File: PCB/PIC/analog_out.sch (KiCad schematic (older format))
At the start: 29 parts, among them J19 TB_1X2, Q1 PBSS5240XF, Q14 BC817-40, U18 LM358, U21 MCP6022

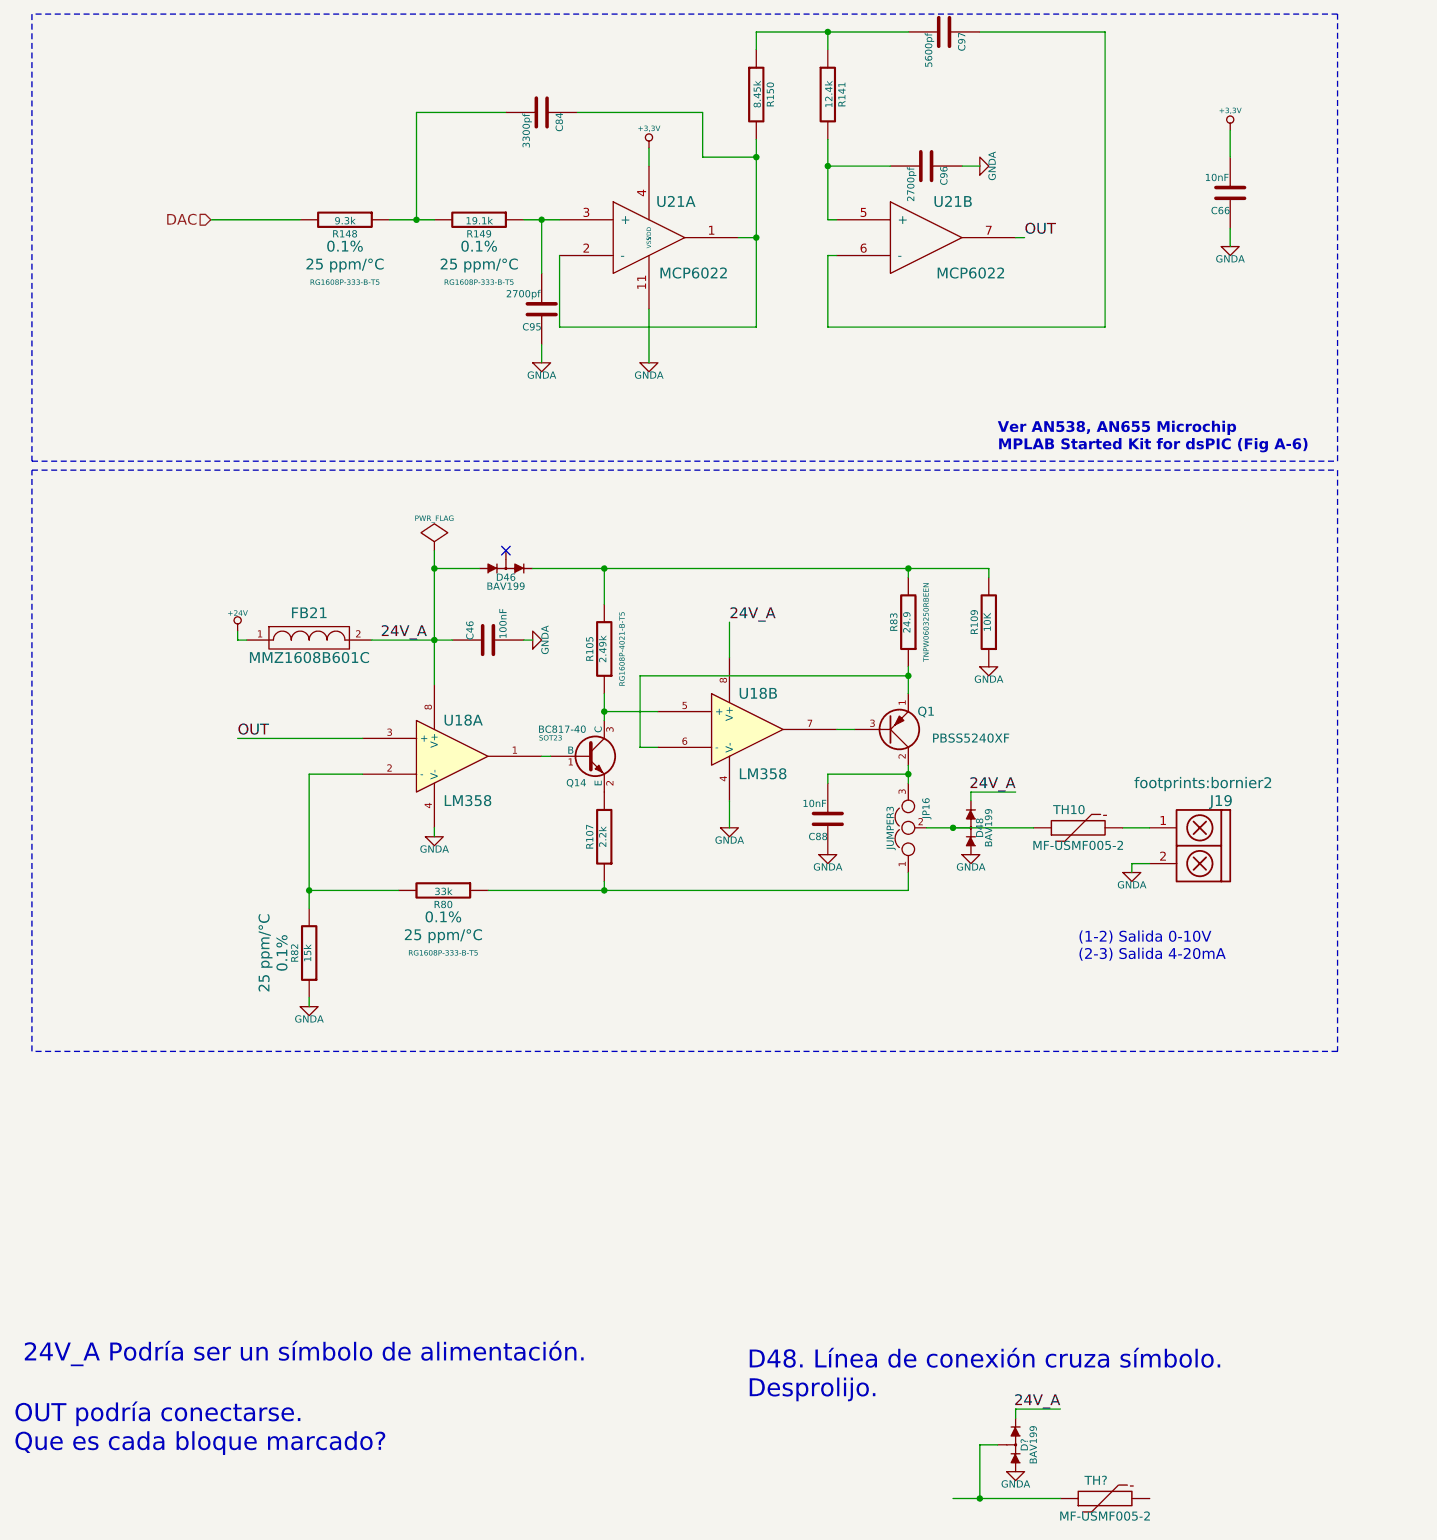
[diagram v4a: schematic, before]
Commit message: elimino conector salida reles
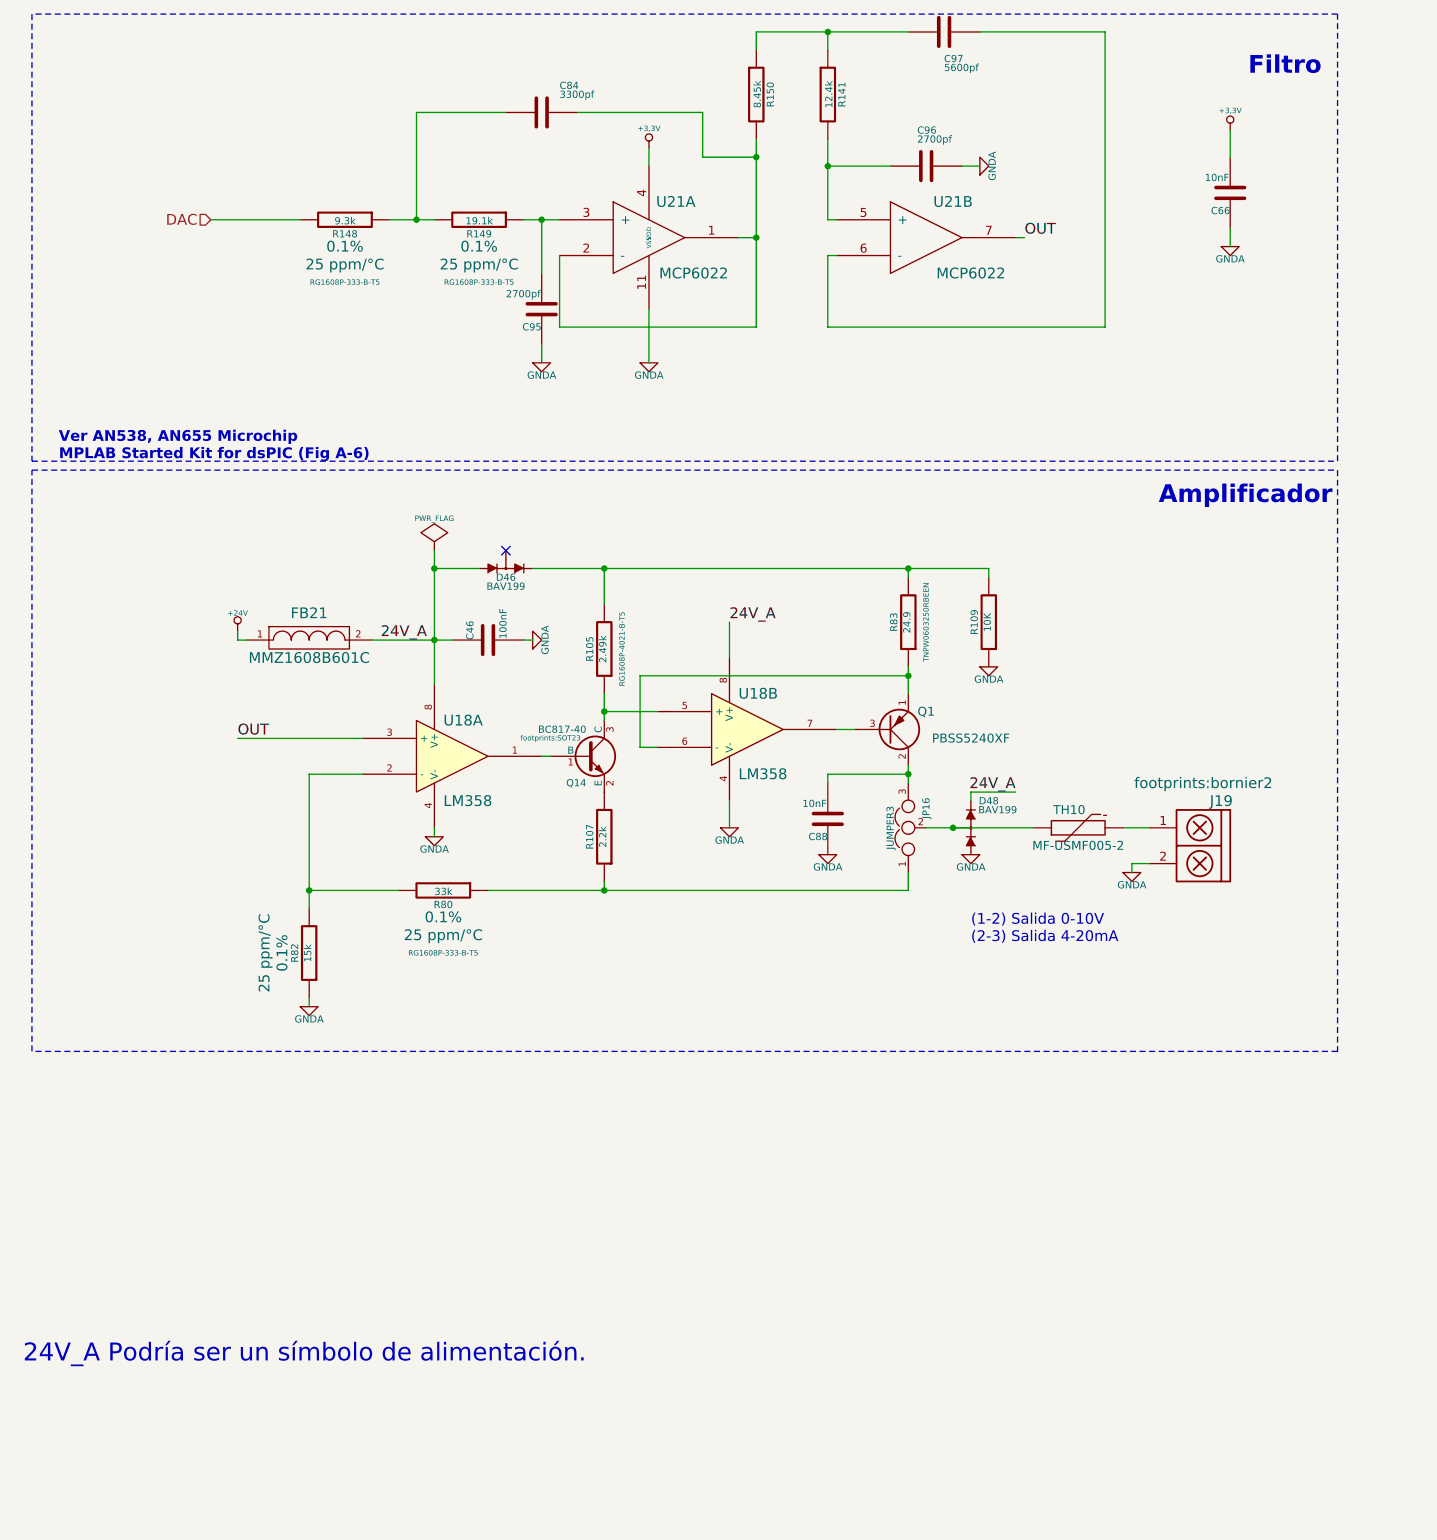
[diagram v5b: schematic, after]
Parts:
- removed D?: BAV199, symbol BAV199
- removed TH?: MF-USMF005-2, symbol THERMISTOR
- C46, C66, C84, C88: footprint ~ -> Capacitors_SMD:C_0603
- C95, C96, C97, FB21, JP16, U21: footprint ~ -> (none)
- Q14: footprint SOT23 -> footprints:SOT23
- R105, R107, R109, R141, R148, R149, R150, R80, R82, R83: footprint ~ -> Resistors_SMD:R_0603
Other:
- note added: "Amplificador"
- note added: "Filtro\n"
- note removed: "D48. Línea de conexión cruza símbolo.\nDesprolijo."
- note removed: "OUT podría conectarse.\nQue es cada bloque marcado?"
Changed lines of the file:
@@
 F 0 "C46" H 5000 4300 40  0000 L CNN
 F 1 "100nF" H 5006 4115 40  0000 L CNN
-F 2 "~" H 5038 4050 30  0000 C CNN
+F 2 "Capacitors_SMD:C_0603" H 5038 4050 30  0001 C CNN
 F 3 "~" H 5000 4200 60  0000 C CNN
 	1    5000 4200
@@
 F 0 "R80" V 4830 5600 40  0000 C CNN
 F 1 "33k" V 4757 5601 40  0000 C CNN
-F 2 "~" V 4680 5600 30  0000 C CNN
+F 2 "Resistors_SMD:R_0603" V 4680 5600 30  0001 C CNN
 F 3 "RG1608P-333-B-T5" V 5100 5600 30  0000 C CNN
 F 4 "0.1%" V 4900 5600 60  0000 C CNN "Tol"
@@
 F 0 "R82" V 4080 5950 40  0000 C CNN
 F 1 "15k" V 4007 5951 40  0000 C CNN
-F 2 "~" V 3930 5950 30  0000 C CNN
+F 2 "Resistors_SMD:R_0603" V 3930 5950 30  0001 C CNN
 F 3 "~" H 4000 5950 30  0000 C CNN
 F 4 "0.1%" V 4150 5950 60  0000 C CNN "Tol"
@@
 F 0 "U18" H 4750 5050 60  0000 L CNN
 F 1 "LM358" H 4750 4600 60  0000 L CNN
-F 2 "" H 4800 4850 60  0000 C CNN
+F 2 "" H 4800 4850 60  0001 C CNN
 F 3 "" H 4800 4850 60  0000 C CNN
 	1    4800 4850
@@
 F 0 "FB21" H 4000 4350 60  0000 C CNN
 F 1 "MMZ1608B601C" H 4000 4100 60  0000 C CNN
-F 2 "~" H 4000 4200 60  0000 C CNN
+F 2 "" H 4000 4200 60  0001 C CNN
 F 3 "~" H 4000 4200 60  0000 C CNN
 	1    4000 4200
@@
 F 0 "U18" H 6400 4900 60  0000 L CNN
 F 1 "LM358" H 6400 4450 60  0000 L CNN
-F 2 "" H 6450 4700 60  0000 C CNN
+F 2 "" H 6450 4700 60  0001 C CNN
 F 3 "" H 6450 4700 60  0000 C CNN
 	2    6450 4700
@@
 F 0 "Q14" H 5550 4701 40  0000 R CNN
 F 1 "BC817-40" H 5550 5000 40  0000 R CNN
-F 2 "SOT23" H 5350 4952 29  0000 C CNN
+F 2 "footprints:SOT23" H 5350 4952 29  0000 C CNN
 F 3 "~" H 5550 4850 60  0000 C CNN
 	1    5550 4850
@@
 F 0 "R107" V 5730 5300 40  0000 C CNN
 F 1 "2.2k" V 5657 5301 40  0000 C CNN
-F 2 "~" V 5580 5300 30  0000 C CNN
+F 2 "Resistors_SMD:R_0603" V 5580 5300 30  0001 C CNN
 F 3 "~" H 5650 5300 30  0000 C CNN
 	1    5650 5300
@@
 F 0 "R105" V 5730 4250 40  0000 C CNN
 F 1 "2.49k" V 5657 4251 40  0000 C CNN
-F 2 "~" V 5580 4250 30  0000 C CNN
+F 2 "Resistors_SMD:R_0603" V 5580 4250 30  0001 C CNN
 F 3 "RG1608P-4021-B-T5" V 5550 4250 30  0000 C CNN
 	1    5650 4250
@@
 F 0 "R83" V 7430 4100 40  0000 C CNN
 F 1 "24.9" V 7357 4101 40  0000 C CNN
-F 2 "~" V 7280 4100 30  0000 C CNN
+F 2 "Resistors_SMD:R_0603" V 7280 4100 30  0001 C CNN
 F 3 "TNPW0603250RBEEN" V 7250 4100 30  0000 C CNN
 	1    7350 4100
@@
 F 0 "JP16" H 7400 5150 40  0000 L CNN
 F 1 "JUMPER3" H 7350 5350 40  0000 C CNN
-F 2 "~" H 7350 5250 60  0000 C CNN
+F 2 "" H 7350 5250 60  0001 C CNN
 F 3 "~" H 7350 5250 60  0000 C CNN
 	1    7350 5250
 	0    -1   -1   0
 $EndComp
-Text Notes 8300 6000 0    60   ~ 0
+Text Notes 7700 5900 0    60   ~ 0
 (1-2) Salida 0-10V\n(2-3) Salida 4-20mA
 $Comp
@@
 F 0 "R109" V 7880 4100 40  0000 C CNN
 F 1 "10K" V 7807 4101 40  0000 C CNN
-F 2 "~" V 7730 4100 30  0000 C CNN
+F 2 "Resistors_SMD:R_0603" V 7730 4100 30  0001 C CNN
 F 3 "~" H 7800 4100 30  0000 C CNN
 	1    7800 4100
@@
 U 1 1 532CF81C
 P 7700 5250
-F 0 "D48" H 7700 5200 40  0000 C CNN
-F 1 "BAV199" H 7700 5150 40  0000 C CNN
-F 2 "" H 7700 5250 60  0000 C CNN
+F 0 "D48" V 7850 5150 40  0000 C CNN
+F 1 "BAV199" V 7800 5100 40  0000 C CNN
+F 2 "" H 7700 5250 60  0001 C CNN
 F 3 "" H 7700 5250 60  0000 C CNN
 	1    7700 5250
@@
 F 0 "C88" H 6900 5300 40  0000 L CNN
 F 1 "10nF" H 6906 5115 40  0000 L CNN
-F 2 "~" H 6938 5050 30  0000 C CNN
+F 2 "Capacitors_SMD:C_0603" H 6938 5050 30  0001 C CNN
 F 3 "~" H 6900 5200 60  0000 C CNN
 	1    6900 5200
@@
 F 0 "D46" H 5100 3750 40  0000 C CNN
 F 1 "BAV199" H 5100 3700 40  0000 C CNN
-F 2 "" H 5100 3800 60  0000 C CNN
+F 2 "" H 5100 3800 60  0001 C CNN
 F 3 "" H 5100 3800 60  0000 C CNN
 	1    5100 3800
@@
 F 0 "TH10" V 8400 5300 50  0000 C CNN
 F 1 "MF-USMF005-2" V 8200 5250 50  0000 C CNN
-F 2 "" H 8300 5250 60  0000 C CNN
+F 2 "" H 8300 5250 60  0001 C CNN
 F 3 "~" H 8300 5250 60  0000 C CNN
 	1    8300 5250
@@
 F 0 "Q1" H 7450 4600 50  0000 C CNN
 F 1 "PBSS5240XF" H 7700 4750 50  0000 C CNN
-F 2 "" H 7650 4650 60  0000 C CNN
+F 2 "" H 7650 4650 60  0001 C CNN
 F 3 "~" H 7250 4700 60  0000 C CNN
 	1    7250 4700
@@
 F 0 "R141" V 6980 1150 40  0000 C CNN
 F 1 "12.4k" V 6907 1151 40  0000 C CNN
-F 2 "~" V 6830 1150 30  0000 C CNN
+F 2 "Resistors_SMD:R_0603" V 6830 1150 30  0001 C CNN
 F 3 "~" H 6900 1150 30  0000 C CNN
 	1    6900 1150
@@
 F 0 "C66" H 9150 1800 40  0000 L CNN
 F 1 "10nF" H 9156 1615 40  0000 L CNN
-F 2 "~" H 9188 1550 30  0000 C CNN
+F 2 "Capacitors_SMD:C_0603" H 9188 1550 30  0001 C CNN
 F 3 "~" H 9150 1700 60  0000 C CNN
 	1    9150 1700
@@
 	1    0    0    -1
 $EndComp
-Text Notes 7850 3150 0    60   ~ 12
+Text Notes 2600 3200 0    60   ~ 12
 Ver AN538, AN655 Microchip\nMPLAB Started Kit for dsPIC (Fig A-6) \n
 $Comp
@@
 F 0 "R149" V 5030 1850 40  0000 C CNN
 F 1 "19.1k" V 4957 1851 40  0000 C CNN
-F 2 "~" V 4880 1850 30  0000 C CNN
+F 2 "Resistors_SMD:R_0603" V 4880 1850 30  0001 C CNN
 F 3 "RG1608P-333-B-T5" V 5300 1850 30  0000 C CNN
 F 4 "0.1%" V 5100 1850 60  0000 C CNN "Tol"
@@
 F 0 "R148" V 4280 1850 40  0000 C CNN
 F 1 "9.3k" V 4207 1851 40  0000 C CNN
-F 2 "~" V 4130 1850 30  0000 C CNN
+F 2 "Resistors_SMD:R_0603" V 4130 1850 30  0001 C CNN
 F 3 "RG1608P-333-B-T5" V 4550 1850 30  0000 C CNN
 F 4 "0.1%" V 4350 1850 60  0000 C CNN "Tol"
@@
 F 0 "C95" H 5300 2450 40  0000 L CNN
 F 1 "2700pf" H 5306 2265 40  0000 L CNN
-F 2 "~" H 5338 2200 30  0000 C CNN
+F 2 "" H 5338 2200 30  0001 C CNN
 F 3 "~" H 5300 2350 60  0000 C CNN
 	1    5300 2350
@@
 F 0 "R150" V 6580 1150 40  0000 C CNN
 F 1 "8.45k" V 6507 1151 40  0000 C CNN
-F 2 "~" V 6430 1150 30  0000 C CNN
+F 2 "Resistors_SMD:R_0603" V 6430 1150 30  0001 C CNN
 F 3 "~" H 6500 1150 30  0000 C CNN
 	1    6500 1150
@@
 U 1 1 543D3E99
 P 7550 800
-F 0 "C97" H 7550 900 40  0000 L CNN
-F 1 "5600pf" H 7556 715 40  0000 L CNN
-F 2 "~" H 7588 650 30  0000 C CNN
+F 0 "C97" V 7700 800 40  0000 L CNN
+F 1 "5600pf" V 7750 800 40  0000 L CNN
+F 2 "" H 7588 650 30  0001 C CNN
 F 3 "~" H 7550 800 60  0000 C CNN
 	1    7550 800
@@
 U 1 1 543D3E9F
 P 7450 1550
-F 0 "C96" H 7450 1650 40  0000 L CNN
-F 1 "2700pf" H 7456 1465 40  0000 L CNN
-F 2 "~" H 7488 1400 30  0000 C CNN
+F 0 "C96" V 7250 1500 40  0000 L CNN
+F 1 "2700pf" V 7300 1500 40  0000 L CNN
+F 2 "" H 7488 1400 30  0001 C CNN
 F 3 "~" H 7450 1550 60  0000 C CNN
 	1    7450 1550
@@
 F 0 "U21" H 6050 2150 60  0000 C CNN
 F 1 "MCP6022" H 6150 1750 60  0000 C CNN
-F 2 "~" H 5900 1950 60  0000 C CNN
+F 2 "" H 5900 1950 60  0001 C CNN
 F 3 "~" H 5900 1950 60  0000 C CNN
 	1    5900 1950
@@
 F 0 "U21" H 7600 2150 60  0000 C CNN
 F 1 "MCP6022" H 7700 1750 60  0000 C CNN
-F 2 "~" H 7450 1950 60  0000 C CNN
+F 2 "" H 7450 1950 60  0001 C CNN
 F 3 "~" H 7450 1950 60  0000 C CNN
 	2    7450 1950
@@
 U 1 1 543D3C4B
 P 5300 1250
-F 0 "C84" H 5300 1350 40  0000 L CNN
-F 1 "3300pf" H 5306 1165 40  0000 L CNN
-F 2 "~" H 5338 1100 30  0000 C CNN
+F 0 "C84" V 5150 1350 40  0000 L CNN
+F 1 "3300pf" V 5200 1350 40  0000 L CNN
+F 2 "Capacitors_SMD:C_0603" H 5338 1100 30  0001 C CNN
 F 3 "~" H 5300 1250 60  0000 C CNN
 	1    5300 1250
@@
 Wire Wire Line
 	6900 1400 6900 1850
-Text Notes 6450 8450 0    100  ~ 0
-D48. Línea de conexión cruza símbolo.\nDesprolijo.
-$Comp
-L BAV199 D?
-U 1 1 576DED47
-P 7950 8700
-F 0 "D?" H 7950 8650 40  0000 C CNN
-F 1 "BAV199" H 7950 8600 40  0000 C CNN
-F 2 "" H 7950 8700 60  0000 C CNN
-F 3 "" H 7950 8700 60  0000 C CNN
-	1    7950 8700
-	0    -1   -1   0
-$EndComp
-$Comp
-L GNDA-RESCUE-ciaa-pic #PWR0173
-U 1 1 576DED4D
-P 7950 8850
-F 0 "#PWR0173" H 7950 8850 40  0001 C CNN
-F 1 "GNDA" H 7950 8780 40  0000 C CNN
-F 2 "" H 7950 8850 60  0000 C CNN
-F 3 "" H 7950 8850 60  0000 C CNN
-	1    7950 8850
-	1    0    0    -1
-$EndComp
-Text Label 8200 8500 2    60   ~ 0
-24V_A
-$Comp
-L THERMISTOR TH?
-U 1 1 576DED54
-P 8450 9000
-F 0 "TH?" V 8550 9050 50  0000 C CNN
-F 1 "MF-USMF005-2" V 8350 9000 50  0000 C CNN
-F 2 "" H 8450 9000 60  0000 C CNN
-F 3 "~" H 8450 9000 60  0000 C CNN
-	1    8450 9000
-	0    -1   -1   0
-$EndComp
-Wire Wire Line
-	7600 9000 8200 9000
-Connection ~ 7750 9000
-Wire Wire Line
-	8200 8500 7950 8500
-Wire Wire Line
-	7950 8500 7950 8550
-Wire Wire Line
-	7850 8700 7750 8700
-Wire Wire Line
-	7750 8700 7750 9000
 Text Notes 2400 8250 0    100  ~ 0
 24V_A Podría ser un símbolo de alimentación.
-Text Notes 2350 8750 0    100  ~ 0
-OUT podría conectarse.\nQue es cada bloque marcado?
+Text Notes 9250 1050 0    99   ~ 20
+Filtro\n
+Text Notes 8750 3450 0    99   ~ 20
+Amplificador
 $EndSCHEMATC
